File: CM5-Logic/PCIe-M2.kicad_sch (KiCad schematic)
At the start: 24 parts, among them J15 Bus_M.2_Socket_M, M1 M.2 Solder Nut, M2 M.2 Solder Nut, M3 M.2 Solder Nut, M4 M.2 Solder Nut, M5 M.2 Screw, U10 AP3441SHE-7B, U11 ASEK-32.768KHZ-L-R-T

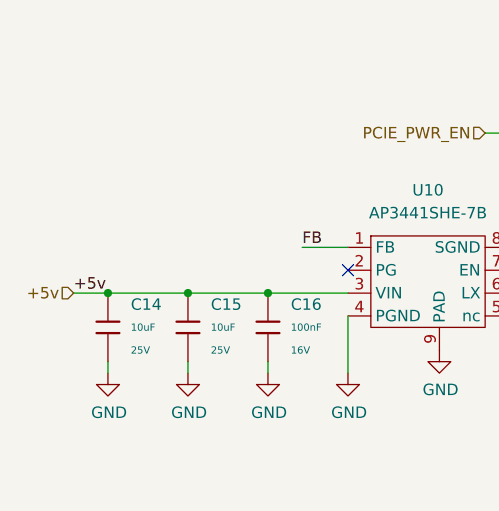
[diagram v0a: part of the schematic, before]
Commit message: fixes a few label issues
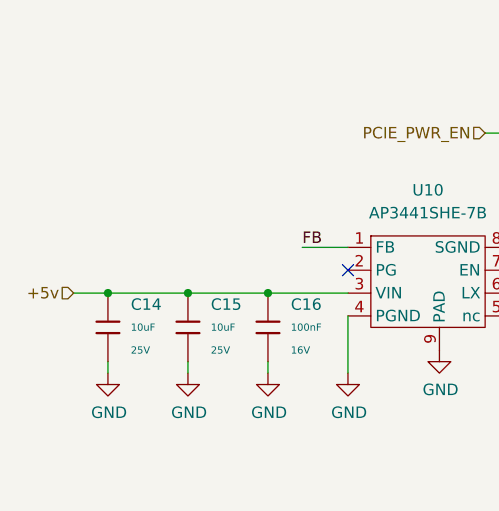
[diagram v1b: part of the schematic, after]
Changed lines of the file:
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@@
-		)
-	)
-	(label "+5v"
-		(at 34.29 167.64 0)
-		(effects
-			(font
-				(size 1.27 1.27)
-			)
-			(justify left bottom)
 		)
 	)

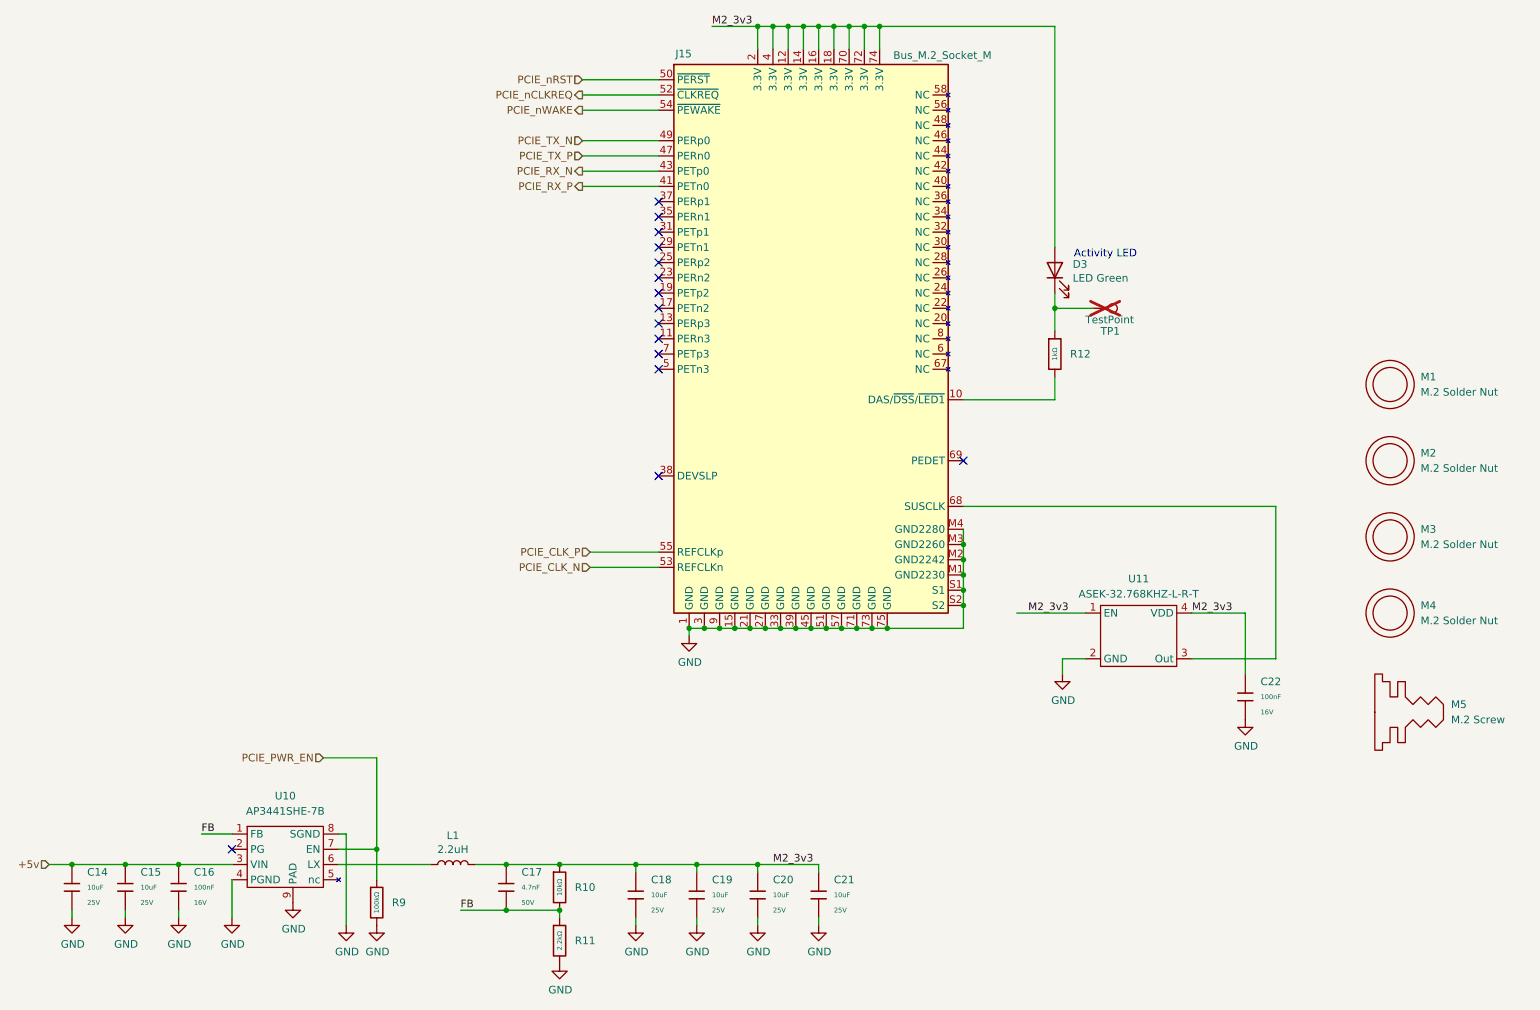
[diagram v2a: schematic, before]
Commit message: changes USB port, adds TMC2209 SilentStepStick footprint, redoes PCB Layout
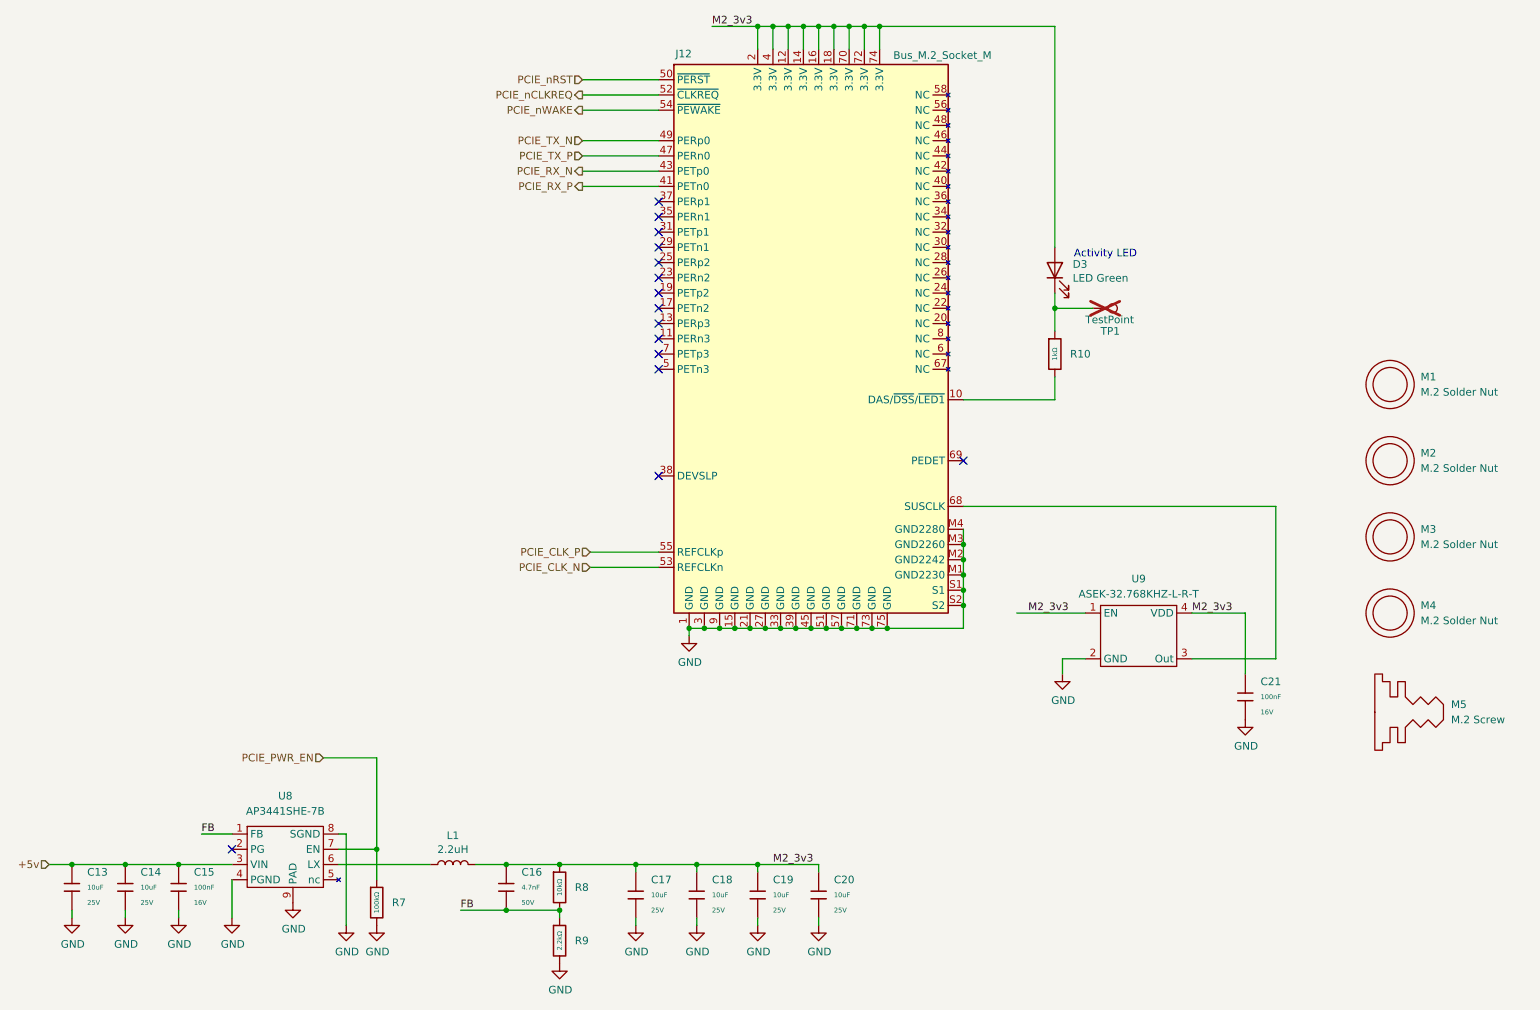
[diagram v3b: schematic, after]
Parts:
- renumbered C14 to C13, C15 to C14, C16 to C15, C17 to C16, C18 to C17, C19 to C18, C20 to C19, C21 to C20, C22 to C21, J15 to J12, R12 to R10, R9 to R7, R10 to R8, R11 to R9, U10 to U8, U11 to U9
